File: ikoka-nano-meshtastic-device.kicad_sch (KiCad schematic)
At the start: 9 parts, among them J1 Battery, J2 Solar, J3 Qwiic_RA, Q1 Q_PMOS_GSD, U1 Seeed Studio XIAO nRF52840, U2 E22-900M30S

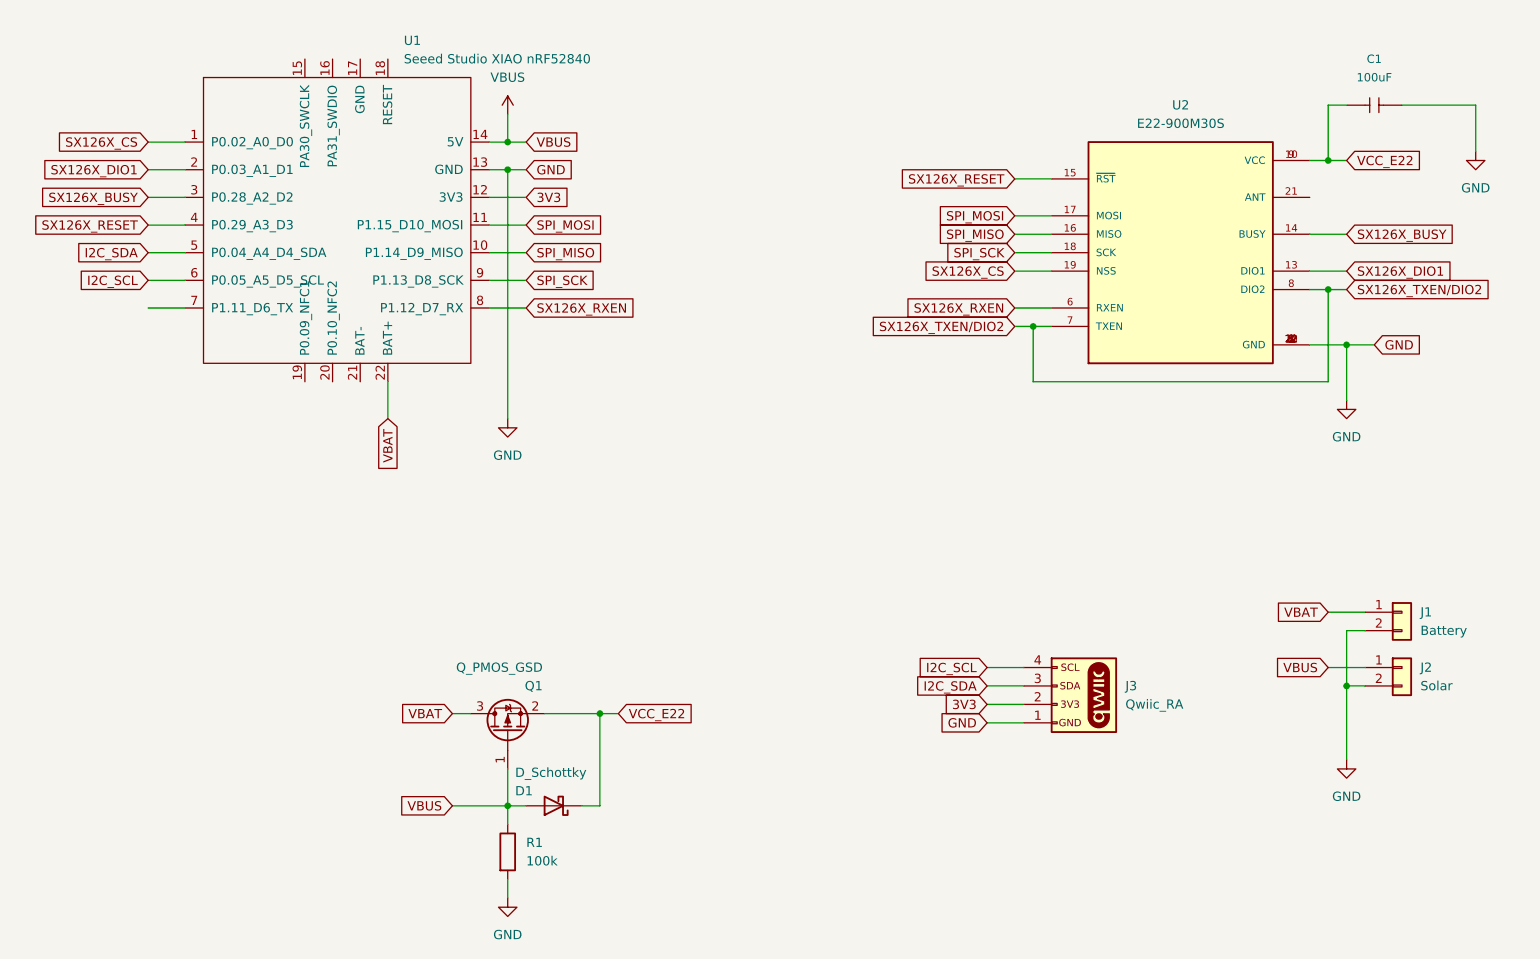
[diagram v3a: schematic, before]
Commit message: Add missing D1 footprint and update PCB; add LCSC part numbers; remove gerbers
Signed-off-by: Andrew Yong <me@ndoo.sg>
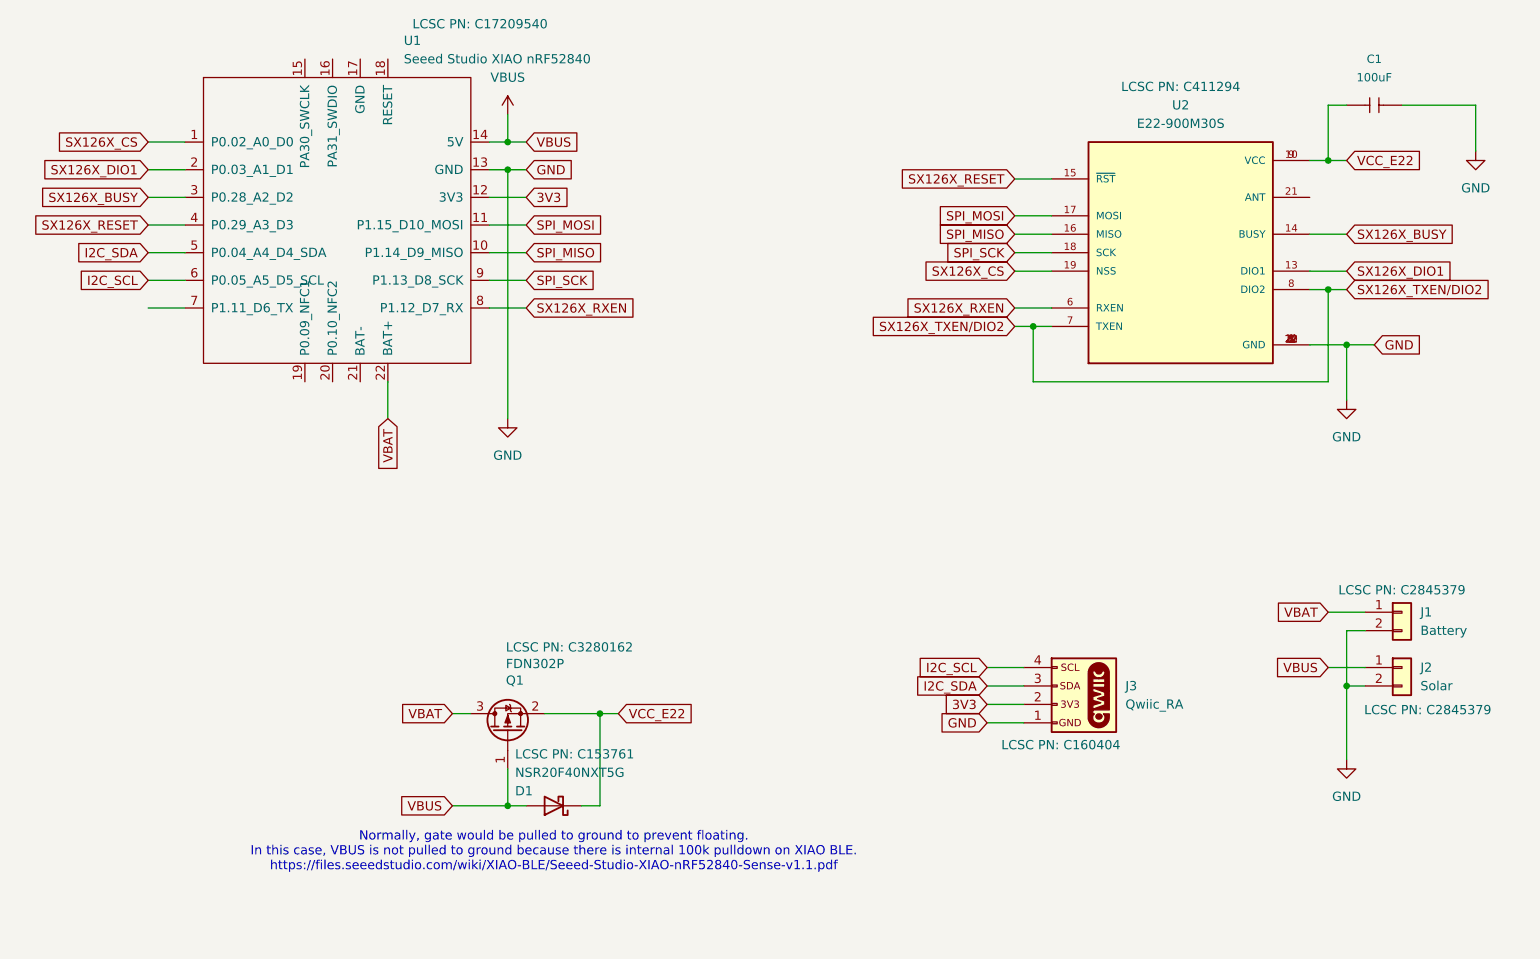
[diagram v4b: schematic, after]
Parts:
- removed R1: 100k, symbol Device:R
- C1: LCSC C77085 -> (none); LCSC PN (none) -> C77085
- D1: value D_Schottky -> NSR20F40NXT5G; footprint (none) -> Diode_SMD:D_0603_1608Metric_Pad1.05x0.95mm_HandSolder; LCSC PN (none) -> C153761
- J1, J2: LCSC PN (none) -> C2845379
- J3: LCSC C160404 -> (none); LCSC PN (none) -> C160404
- Q1: value Q_PMOS_GSD -> FDN302P; LCSC PN (none) -> C3280162
- U1: LCSC C17209540 -> (none); LCSC PN (none) -> C17209540
- U2: LCSC C411294 -> (none); LCSC PN (none) -> C411294
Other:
- note added: "Normally, gate would be pulled to ground to prevent floating. In this case, VBUS is not pulled to ground because there is internal 100k pulldown on XIAO BLE. https://files.seeedstudio.com/wiki/XIAO-BLE/Seeed-Studio-XIAO-nRF52840-Sense-v1.1.pdf"
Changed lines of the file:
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@@
-	(wire
-		(pts
-			(xy 104.14 139.7) (xy 104.14 142.24)
-		)
-		(stroke
-			(width 0)
-			(type default)
-		)
-	)
 	(wire
 		(pts
@@
 	(wire
 		(pts
-			(xy 104.14 149.86) (xy 104.14 152.4)
-		)
-		(stroke
-			(width 0)
-			(type default)
-		)
-	)
-	(wire
-		(pts
 			(xy 219.71 76.2) (xy 219.71 83.82)
 		)
@@
 			(width 0)
 			(type default)
+		)
+	)
+	(text "Normally, gate would be pulled to ground to prevent floating.\nIn this case, VBUS is not pulled to ground because there is internal 100k pulldown on XIAO BLE.\nhttps://files.seeedstudio.com/wiki/XIAO-BLE/Seeed-Studio-XIAO-nRF52840-Sense-v1.1.pdf"
+		(exclude_from_sim no)
+		(at 110.49 146.05 0)
+		(effects
+			(font
+				(size 1.27 1.27)
+			)
 		)
 	)
@@
 		(on_board yes)
 		(dnp no)
-		(fields_autoplaced yes)
 		(property "Reference" "J1"
 			(at 229.87 113.0299 0)
@@
 				)
 				(hide yes)
+			)
+		)
+		(property "LCSC PN" "C2845379"
+			(at 227.33 109.982 0)
+			(show_name yes)
+			(effects
+				(font
+					(size 1.27 1.27)
+				)
 			)
 		)
@@
 			)
 		)
-		(property "Value" "D_Schottky"
+		(property "Value" "NSR20F40NXT5G"
 			(at 105.156 135.128 0)
 			(effects
@@
 			)
 		)
-		(property "Footprint" ""
+		(property "Footprint" "Diode_SMD:D_0603_1608Metric_Pad1.05x0.95mm_HandSolder"
 			(at 110.49 139.7 0)
 			(effects
@@
 			)
 		)
-		(property "Datasheet" "~"
+		(property "Datasheet" "https://www.lcsc.com/datasheet/lcsc_datasheet_2410010330_onsemi-NSR20F40NXT5G_C153761.pdf"
 			(at 110.49 139.7 0)
 			(effects
@@
 			)
 		)
-		(property "Description" "Schottky diode"
+		(property "Description" "40V 550mV@2A 2A 0603 Schottky Diodes ROHS"
 			(at 110.49 139.7 0)
 			(effects
@@
 				)
 				(hide yes)
+			)
+		)
+		(property "LCSC PN" "C153761"
+			(at 105.156 132.588 0)
+			(show_name yes)
+			(effects
+				(font
+					(size 1.27 1.27)
+				)
+				(justify right)
 			)
 		)
@@
 		(on_board yes)
 		(dnp no)
-		(fields_autoplaced yes)
 		(property "Reference" "J3"
 			(at 189.23 123.19 0)
@@
 			)
 		)
-		(property "LCSC" "C160404"
-			(at 180.34 123.19 0)
-			(effects
-				(font
-					(size 1.27 1.27)
-				)
-				(hide yes)
+		(property "LCSC PN" "C160404"
+			(at 180.34 131.318 0)
+			(show_name yes)
+			(effects
+				(font
+					(size 1.27 1.27)
+				)
 			)
 		)
@@
 		(dnp no)
 		(property "Reference" "Q1"
-			(at 108.966 123.19 90)
-			(effects
-				(font
-					(size 1.27 1.27)
-				)
-				(justify left)
-			)
-		)
-		(property "Value" "Q_PMOS_GSD"
-			(at 108.966 120.65 90)
-			(effects
-				(font
-					(size 1.27 1.27)
-				)
-				(justify left)
+			(at 103.886 122.428 90)
+			(effects
+				(font
+					(size 1.27 1.27)
+				)
+				(justify right)
+			)
+		)
+		(property "Value" "FDN302P"
+			(at 103.886 120.142 90)
+			(effects
+				(font
+					(size 1.27 1.27)
+				)
+				(justify right)
 			)
 		)
@@
 			)
 		)
-		(property "Datasheet" "~"
+		(property "Datasheet" "https://www.lcsc.com/datasheet/lcsc_datasheet_2410010102_onsemi-FDN302P_C3280162.pdf"
 			(at 104.14 129.54 0)
 			(effects
@@
 			)
 		)
-		(property "Description" "P-MOSFET transistor, gate/source/drain"
+		(property "Description" "20V 2.4A 55mΩ@2.4A,4.5V 500mW 1.5V@250uA 1 Piece P-Channel SOT-23-3 MOSFETs ROHS"
 			(at 104.14 129.54 0)
 			(effects
@@
 				)
 				(hide yes)
+			)
+		)
+		(property "LCSC PN" "C3280162"
+			(at 103.886 117.856 90)
+			(show_name yes)
+			(effects
+				(font
+					(size 1.27 1.27)
+				)
+				(justify right)
 			)
 		)
@@
 		(on_board yes)
 		(dnp no)
-		(fields_autoplaced yes)
 		(property "Reference" "J2"
 			(at 229.87 120.6499 0)
@@
 				)
 				(hide yes)
+			)
+		)
+		(property "LCSC PN" "C2845379"
+			(at 230.886 126.492 0)
+			(show_name yes)
+			(effects
+				(font
+					(size 1.27 1.27)
+				)
 			)
 		)
@@
 	)
 	(symbol
-		(lib_id "Device:R")
-		(at 104.14 146.05 0)
-		(unit 1)
-		(exclude_from_sim no)
-		(in_bom yes)
-		(on_board yes)
-		(dnp no)
-		(fields_autoplaced yes)
-		(property "Reference" "R1"
-			(at 106.68 144.7799 0)
-			(effects
-				(font
-					(size 1.27 1.27)
-				)
-				(justify left)
-			)
-		)
-		(property "Value" "100k"
-			(at 106.68 147.3199 0)
-			(effects
-				(font
-					(size 1.27 1.27)
-				)
-				(justify left)
-			)
-		)
-		(property "Footprint" ""
-			(at 102.362 146.05 90)
-			(effects
-				(font
-					(size 1.27 1.27)
-				)
-				(hide yes)
-			)
-		)
-		(property "Datasheet" "~"
-			(at 104.14 146.05 0)
-			(effects
-				(font
-					(size 1.27 1.27)
-				)
-				(hide yes)
-			)
-		)
-		(property "Description" "Resistor"
-			(at 104.14 146.05 0)
-			(effects
-				(font
-					(size 1.27 1.27)
-				)
-				(hide yes)
-			)
-		)
-		(pin "1"
-		)
-		(pin "2"
-		)
-		(instances
-			(project ""
-				(path "/e83bb9a9-6169-4e6e-a646-f5672e545713"
-					(reference "R1")
-					(unit 1)
-				)
-			)
-		)
-	)
-	(symbol
 		(lib_id "E22-900M30S:E22-900M30S")
 		(at 196.85 63.5 0)
@@
 		(on_board yes)
 		(dnp no)
-		(fields_autoplaced yes)
 		(property "Reference" "U2"
 			(at 196.85 43.18 0)
@@
 			)
 		)
-		(property "Description" "\nSX1262 868/915 MHz 1w SPI LoRa Module\n"
+		(property "Description" "SX1262 868/915 MHz 1w SPI LoRa Module"
 			(at 196.85 63.5 0)
 			(effects
@@
 			)
 		)
-		(property "LCSC" "C411294"
-			(at 196.85 63.5 0)
-			(effects
-				(font
-					(size 1.27 1.27)
-				)
-				(hide yes)
+		(property "LCSC PN" "C411294"
+			(at 196.85 40.64 0)
+			(show_name yes)
+			(effects
+				(font
+					(size 1.27 1.27)
+				)
 			)
 		)
@@
 				(path "/e83bb9a9-6169-4e6e-a646-f5672e545713"
 					(reference "U2")
-					(unit 1)
-				)
-			)
-		)
-	)
-	(symbol
-		(lib_name "GND_2")
-		(lib_id "power:GND")
-		(at 104.14 152.4 0)
-		(unit 1)
-		(exclude_from_sim no)
-		(in_bom yes)
-		(on_board yes)
-		(dnp no)
-		(fields_autoplaced yes)
-		(property "Reference" "#PWR06"
-			(at 104.14 158.75 0)
-			(effects
-				(font
-					(size 1.27 1.27)
-				)
-				(hide yes)
-			)
-		)
-		(property "Value" "GND"
-			(at 104.14 157.48 0)
-			(effects
-				(font
-					(size 1.27 1.27)
-				)
-			)
-		)
-		(property "Footprint" ""
-			(at 104.14 152.4 0)
-			(effects
-				(font
-					(size 1.27 1.27)
-				)
-				(hide yes)
-			)
-		)
-		(property "Datasheet" ""
-			(at 104.14 152.4 0)
-			(effects
-				(font
-					(size 1.27 1.27)
-				)
-				(hide yes)
-			)
-		)
-		(property "Description" "Power symbol creates a global label with name \"GND\" , ground"
-			(at 104.14 152.4 0)
-			(effects
-				(font
-					(size 1.27 1.27)
-				)
-				(hide yes)
-			)
-		)
-		(pin "1"
-		)
-		(instances
-			(project ""
-				(path "/e83bb9a9-6169-4e6e-a646-f5672e545713"
-					(reference "#PWR06")
 					(unit 1)
 				)
@@
 			)
 		)
-		(property "LCSC" "C77085"
+		(property "LCSC PN" "C77085"
 			(at 223.52 43.18 0)
 			(effects
@@
 		(on_board yes)
 		(dnp no)
-		(fields_autoplaced yes)
 		(property "Reference" "U1"
 			(at 89.8241 34.29 0)
@@
 			)
 		)
-		(property "LCSC" "C17209540"
-			(at 81.28 59.69 0)
-			(effects
-				(font
-					(size 1.27 1.27)
-				)
-				(hide yes)
-			)
-		)
+		(property "LCSC PN" "C17209540"
+			(at 100.33 32.004 0)
+			(show_name yes)
+			(effects
+				(font
+					(size 1.27 1.27)
+				)
+			)
+		)

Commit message: Fix part attributes for LCSC PN and make compatible with latest JLCPCB fabrication toolkit
Signed-off-by: Andrew Yong <me@ndoo.sg>
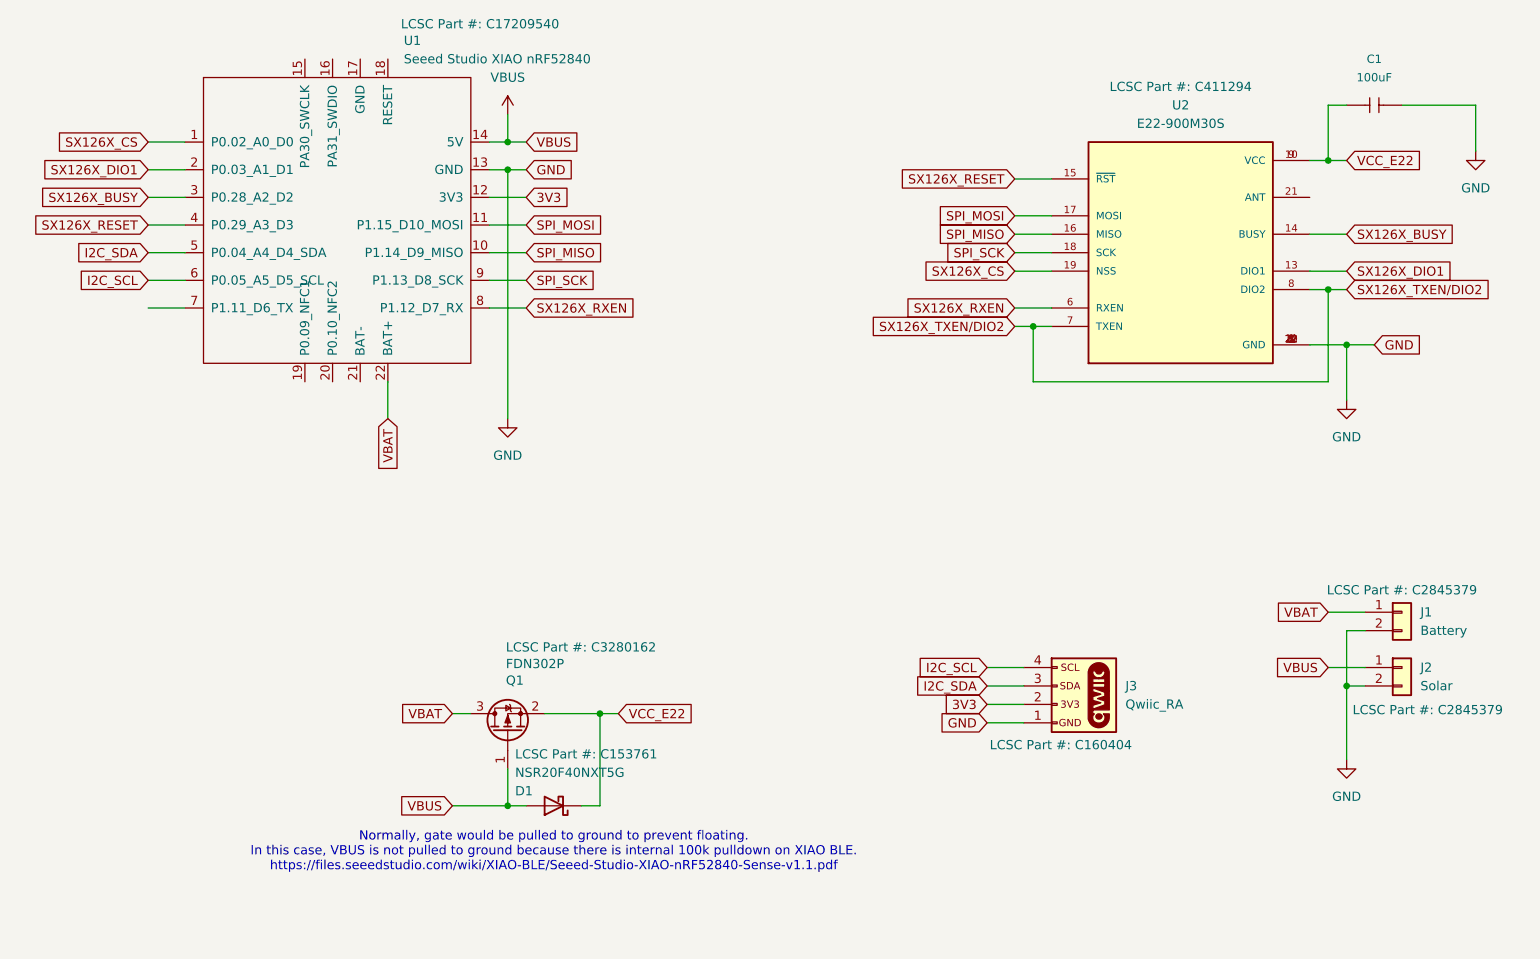
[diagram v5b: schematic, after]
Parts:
- C1: LCSC PN C77085 -> (none); LCSC Part # (none) -> C77085
- D1: LCSC PN C153761 -> (none); LCSC Part # (none) -> C153761
- J1, J2: LCSC PN C2845379 -> (none); LCSC Part # (none) -> C2845379
- J3: LCSC PN C160404 -> (none); LCSC Part # (none) -> C160404
- Q1: LCSC PN C3280162 -> (none); LCSC Part # (none) -> C3280162
- U1: LCSC PN C17209540 -> (none); LCSC Part # (none) -> C17209540
- U2: LCSC PN C411294 -> (none); LCSC Part # (none) -> C411294
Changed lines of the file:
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@@
 			)
 		)
-		(property "LCSC PN" "C2845379"
+		(property "LCSC Part #" "C2845379"
 			(at 227.33 109.982 0)
 			(show_name yes)
@@
 			)
 		)
-		(property "LCSC PN" "C153761"
+		(property "LCSC Part #" "C153761"
 			(at 105.156 132.588 0)
 			(show_name yes)
@@
 			)
 		)
-		(property "LCSC PN" "C160404"
+		(property "LCSC Part #" "C160404"
 			(at 180.34 131.318 0)
 			(show_name yes)
@@
 			)
 		)
-		(property "LCSC PN" "C3280162"
+		(property "LCSC Part #" "C3280162"
 			(at 103.886 117.856 90)
 			(show_name yes)
@@
 			)
 		)
-		(property "LCSC PN" "C2845379"
+		(property "LCSC Part #" "C2845379"
 			(at 230.886 126.492 0)
 			(show_name yes)
@@
 			)
 		)
-		(property "LCSC PN" "C411294"
+		(property "LCSC Part #" "C411294"
 			(at 196.85 40.64 0)
 			(show_name yes)
@@
 			)
 		)
-		(property "LCSC PN" "C77085"
+		(property "LCSC Part #" "C77085"
 			(at 223.52 43.18 0)
 			(effects
@@
 			)
 		)
-		(property "LCSC PN" "C17209540"
+		(property "LCSC Part #" "C17209540"
 			(at 100.33 32.004 0)
 			(show_name yes)

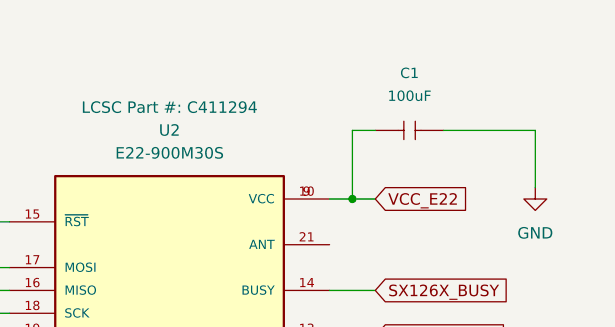
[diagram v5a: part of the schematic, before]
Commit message: Add LCSC PN display for C1, clean up production folder again
Signed-off-by: Andrew Yong <me@ndoo.sg>
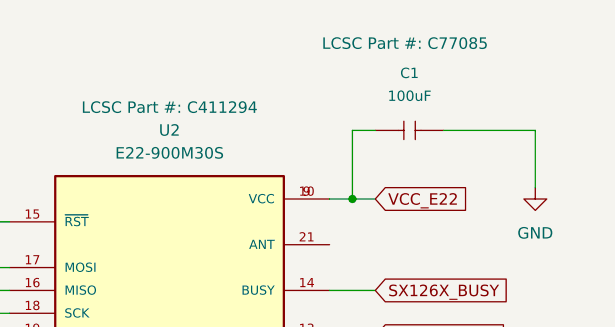
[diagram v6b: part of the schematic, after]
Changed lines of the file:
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@@
 		(on_board yes)
 		(dnp no)
-		(fields_autoplaced yes)
 		(property "Reference" "C1"
 			(at 223.52 36.83 0)
@@
 		)
 		(property "LCSC Part #" "C77085"
-			(at 223.52 43.18 0)
+			(at 223.012 33.528 0)
+			(show_name yes)
 			(effects
 				(font
 					(size 1.27 1.27)
 				)
-				(hide yes)
 			)
 		)
